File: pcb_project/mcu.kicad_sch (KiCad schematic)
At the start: 24 parts, among them J3 Conn_ST_STDC14, SW2 SW_SPDT, SW3 SW_SPST, U2 STM32U595VJTx, Y1 48MHz

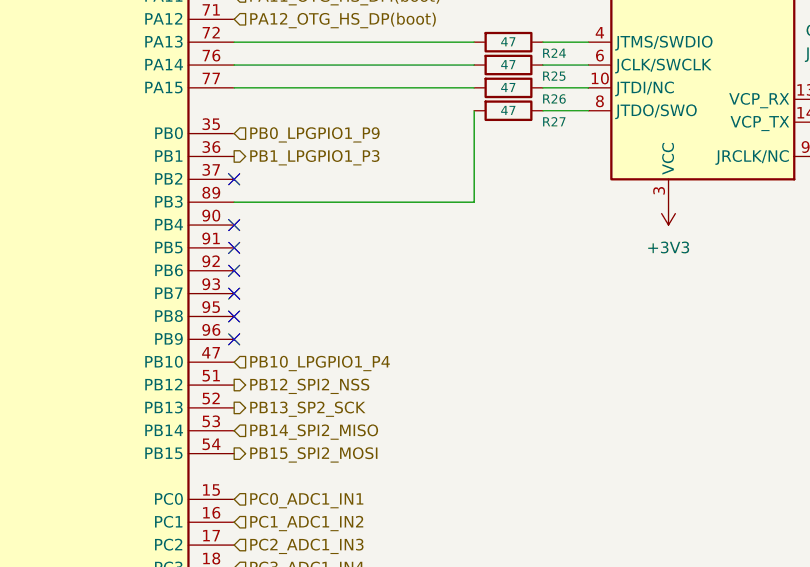
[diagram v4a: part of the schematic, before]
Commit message: Add FPGA DONE AND PROGRAM_B (reset) to MCU GPIO
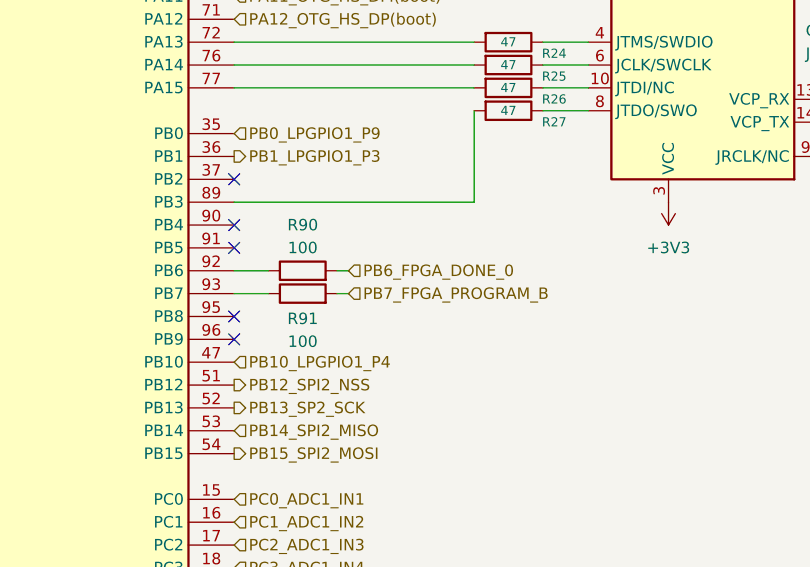
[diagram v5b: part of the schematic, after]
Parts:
- added R90, R91: 100, symbol Device:R
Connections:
- net at U2.92 (PB6): now also R90.1
- net at U2.93 (PB7): now also R91.1
- new net PB6_FPGA_DONE_0: R90.2
- new net PB7_FPGA_PROGRAM_B: R91.2
- no-connect marks 45 -> 43
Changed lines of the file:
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@@
-	)
-	(no_connect
-		(at 124.46 100.33)
 	)
 	(no_connect
@@
 	)
 	(no_connect
-		(at 124.46 97.79)
-	)
-	(no_connect
 		(at 124.46 64.77)
 	)
@@
 	(wire
 		(pts
+			(xy 135.89 97.79) (xy 137.16 97.79)
+		)
+		(stroke
+			(width 0)
+			(type default)
+		)
+	)
+	(wire
+		(pts
 			(xy 73.66 57.15) (xy 78.74 57.15)
 		)
@@
 	(wire
 		(pts
+			(xy 124.46 97.79) (xy 128.27 97.79)
+		)
+		(stroke
+			(width 0)
+			(type default)
+		)
+	)
+	(wire
+		(pts
 			(xy 240.03 36.83) (xy 247.65 36.83)
 		)
@@
 	(wire
 		(pts
+			(xy 124.46 100.33) (xy 128.27 100.33)
+		)
+		(stroke
+			(width 0)
+			(type default)
+		)
+	)
+	(wire
+		(pts
 			(xy 43.18 30.48) (xy 40.64 30.48)
 		)
@@
 		(pts
 			(xy 43.18 39.37) (xy 43.18 30.48)
+		)
+		(stroke
+			(width 0)
+			(type default)
+		)
+	)
+	(wire
+		(pts
+			(xy 135.89 100.33) (xy 137.16 100.33)
 		)
 		(stroke
@@
 		)
 	)
+	(hierarchical_label "PB6_FPGA_DONE_0"
+		(shape input)
+		(at 137.16 97.79 0)
+		(effects
+			(font
+				(size 1.27 1.27)
+			)
+			(justify left)
+		)
+	)
 	(hierarchical_label "PC11_SDMMC1_D3"
 		(shape input)
@@
 			)
 			(justify right)
+		)
+	)
+	(hierarchical_label "PB7_FPGA_PROGRAM_B"
+		(shape input)
+		(at 137.16 100.33 0)
+		(effects
+			(font
+				(size 1.27 1.27)
+			)
+			(justify left)
 		)
 	)
@@
 					(unit 1)
 				)
+			)
+		)
+	)
+	(symbol
+		(lib_id "Device:R")
+		(at 132.08 97.79 90)
+		(unit 1)
+		(exclude_from_sim no)
+		(in_bom yes)
+		(on_board yes)
+		(dnp no)
+		(property "Reference" "R90"
+			(at 132.08 92.71 90)
+			(effects
+				(font
+					(size 1.27 1.27)
+				)
+			)
+		)
+		(property "Value" "100"
+			(at 132.08 95.25 90)
+			(effects
+				(font
+					(size 1.27 1.27)
+				)
+			)
+		)
+		(property "Footprint" ""
+			(at 132.08 99.568 90)
+			(effects
+				(font
+					(size 1.27 1.27)
+				)
+				(hide yes)
+			)
+		)
+		(property "Datasheet" "~"
+			(at 132.08 97.79 0)
+			(effects
+				(font
+					(size 1.27 1.27)
+				)
+				(hide yes)
+			)
+		)
+		(property "Description" "Resistor"
+			(at 132.08 97.79 0)
+			(effects
+				(font
+					(size 1.27 1.27)
+				)
+				(hide yes)
+			)
+		)
+		(pin "1"
+		)
+		(pin "2"
+		)
+		(instances
+			(project ""
+				(path "/98f80f66-4595-4d0f-90ca-59b2db6f447b/1a3eaa4f-d49c-486a-8882-cdef72ae86f4"
+					(reference "R90")
+					(unit 1)
+				)
+			)
+		)
+	)
+	(symbol
+		(lib_id "Device:R")
+		(at 132.08 100.33 90)
+		(unit 1)
+		(exclude_from_sim no)
+		(in_bom yes)
+		(on_board yes)
+		(dnp no)
+		(property "Reference" "R91"
+			(at 132.08 103.124 90)
+			(effects
+				(font
+					(size 1.27 1.27)
+				)
+			)
+		)
+		(property "Value" "100"
+			(at 132.08 105.664 90)
+			(effects
+				(font
+					(size 1.27 1.27)
+				)
+			)
+		)
+		(property "Footprint" ""
+			(at 132.08 102.108 90)
+			(effects
+				(font
+					(size 1.27 1.27)
+				)
+				(hide yes)
+			)
+		)
+		(property "Datasheet" "~"
+			(at 132.08 100.33 0)
+			(effects
+				(font
+					(size 1.27 1.27)
+				)
+				(hide yes)
+			)
+		)
+		(property "Description" "Resistor"
+			(at 132.08 100.33 0)
+			(effects
+				(font
+					(size 1.27 1.27)
+				)
+				(hide yes)
+			)
+		)
+		(pin "1"
+		)
+		(pin "2"
+		)
+		(instances
+			(project ""
+				(path "/98f80f66-4595-4d0f-90ca-59b2db6f447b/1a3eaa4f-d49c-486a-8882-cdef72ae86f4"
+					(reference "R91")
+					(unit 1)
+				)

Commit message: Add most footprints, missing some inductors and 3 buttons
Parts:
- C37, C38: footprint (none) -> Capacitor_SMD:C_0603_1608Metric_Pad1.08x0.95mm_HandSolder
- C39, C41, C42: footprint (none) -> Capacitor_SMD:C_0805_2012Metric_Pad1.18x1.45mm_HandSolder
- C40: footprint (none) -> Capacitor_SMD:C_1206_3216Metric_Pad1.33x1.80mm_HandSolder
- J3: footprint (none) -> Connector_PinHeader_1.27mm:PinHeader_2x07_P1.27mm_Vertical
- R23, R24, R25, R26, R27, R90, R91: footprint (none) -> Resistor_SMD:R_0805_2012Metric_Pad1.20x1.40mm_HandSolder
- Y1: footprint (none) -> Project_Footprints:OSCCC320X250X60N
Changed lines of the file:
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@@
 			)
 		)
-		(property "Footprint" ""
+		(property "Footprint" "Resistor_SMD:R_0805_2012Metric_Pad1.20x1.40mm_HandSolder"
 			(at 154.94 75.692 90)
 			(effects
@@
 			)
 		)
-		(property "Footprint" ""
+		(property "Footprint" "Capacitor_SMD:C_0805_2012Metric_Pad1.18x1.45mm_HandSolder"
 			(at 79.7052 163.83 0)
 			(effects
@@
 			)
 		)
-		(property "Footprint" ""
+		(property "Footprint" "Capacitor_SMD:C_1206_3216Metric_Pad1.33x1.80mm_HandSolder"
 			(at 221.9452 36.83 0)
 			(effects
@@
 			)
 		)
-		(property "Footprint" ""
+		(property "Footprint" "Resistor_SMD:R_0805_2012Metric_Pad1.20x1.40mm_HandSolder"
 			(at 132.08 99.568 90)
 			(effects
@@
 			)
 		)
-		(property "Footprint" ""
+		(property "Footprint" "Resistor_SMD:R_0805_2012Metric_Pad1.20x1.40mm_HandSolder"
 			(at 132.08 102.108 90)
 			(effects
@@
 			)
 		)
-		(property "Footprint" ""
+		(property "Footprint" "Capacitor_SMD:C_0805_2012Metric_Pad1.18x1.45mm_HandSolder"
 			(at 221.9452 83.82 0)
 			(effects
@@
 			)
 		)
-		(property "Footprint" ""
+		(property "Footprint" "Capacitor_SMD:C_0603_1608Metric_Pad1.08x0.95mm_HandSolder"
 			(at 33.02 55.5752 0)
 			(effects
@@
 			)
 		)
-		(property "Footprint" ""
+		(property "Footprint" "Capacitor_SMD:C_0805_2012Metric_Pad1.18x1.45mm_HandSolder"
 			(at 221.9452 60.96 0)
 			(effects
@@
 			)
 		)
-		(property "Footprint" ""
+		(property "Footprint" "Capacitor_SMD:C_0603_1608Metric_Pad1.08x0.95mm_HandSolder"
 			(at 33.02 31.4452 0)
 			(effects
@@
 			)
 		)
-		(property "Footprint" ""
+		(property "Footprint" "Resistor_SMD:R_0805_2012Metric_Pad1.20x1.40mm_HandSolder"
 			(at 154.94 78.232 90)
 			(effects
@@
 			)
 		)
-		(property "Footprint" ""
+		(property "Footprint" "Connector_PinHeader_1.27mm:PinHeader_2x07_P1.27mm_Vertical"
 			(at 176.53 72.39 0)
 			(effects
@@
 			)
 		)
-		(property "Footprint" ""
+		(property "Footprint" "Resistor_SMD:R_0805_2012Metric_Pad1.20x1.40mm_HandSolder"
 			(at 154.94 70.612 90)
 			(effects
@@
 			)
 		)
-		(property "Footprint" ""
+		(property "Footprint" "Resistor_SMD:R_0805_2012Metric_Pad1.20x1.40mm_HandSolder"
 			(at 154.94 73.152 90)
 			(effects
@@
 			)
 		)
-		(property "Footprint" ""
+		(property "Footprint" "Project_Footprints:OSCCC320X250X60N"
 			(at 43.18 43.18 0)
 			(effects
@@
 			)
 		)
-		(property "Footprint" ""
+		(property "Footprint" "Resistor_SMD:R_0805_2012Metric_Pad1.20x1.40mm_HandSolder"
 			(at 69.85 58.928 90)
 			(effects

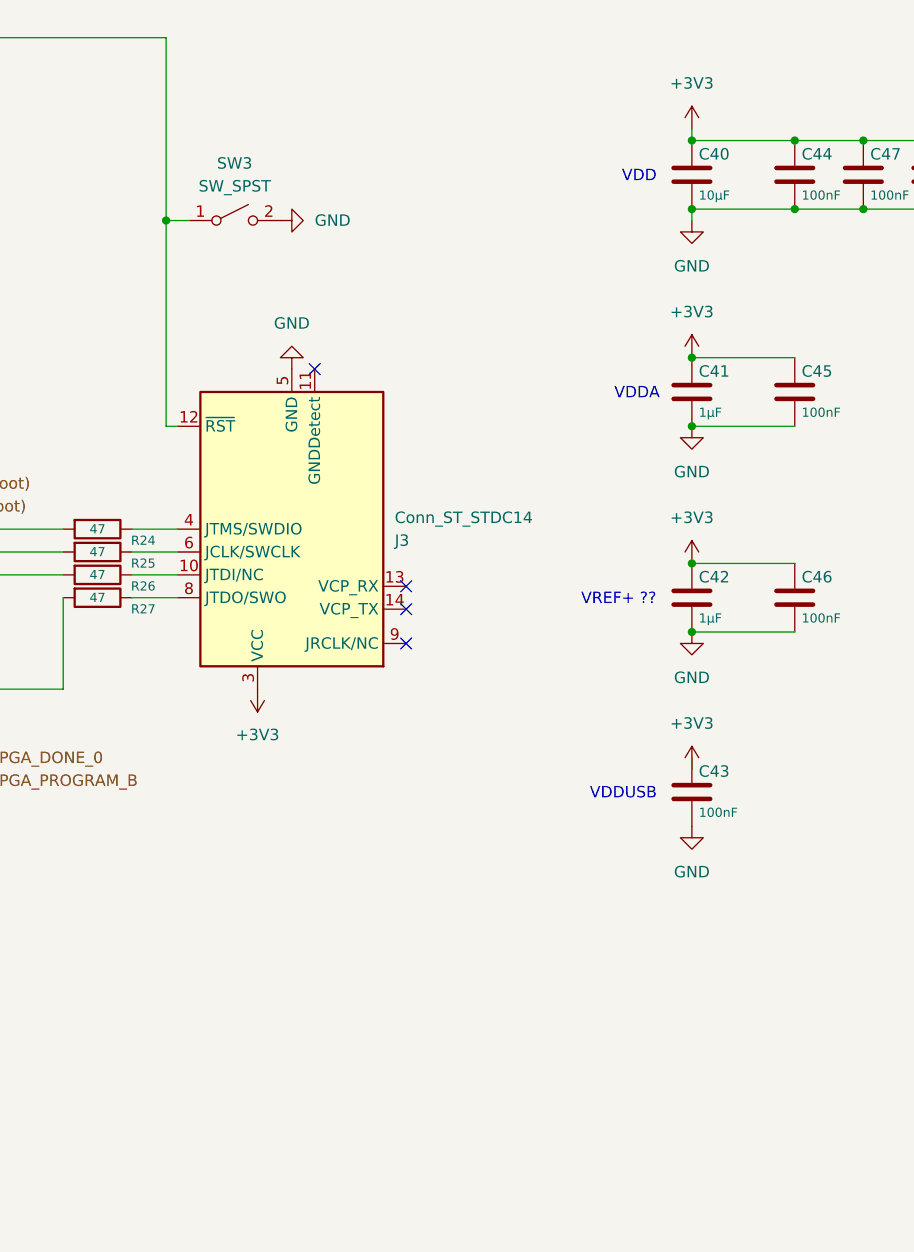
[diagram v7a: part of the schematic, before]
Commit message: Add debouncing capasitor for MCU reset button
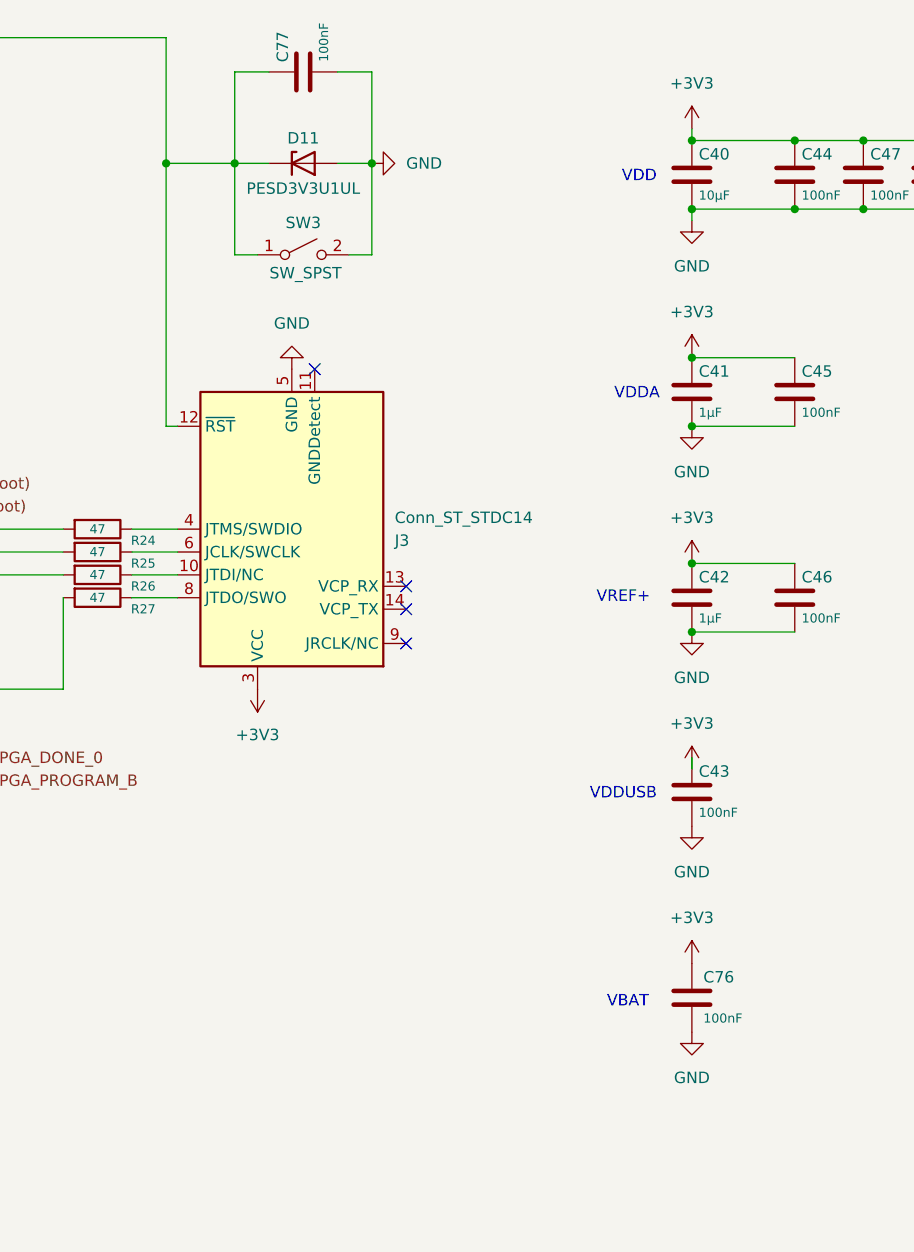
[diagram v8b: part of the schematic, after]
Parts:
- added C76, C77: 100nF, symbol Device:C
- added D11: PESD3V3U1UL, Diode_SMD:D_SOD-882, symbol Diode:PESD3V3U1UL
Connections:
- net +3V3: now also C76.1
- net GND: now also C76.2, C77.2, D11.2 (A)
- net at J3.12 (~{RST}), SW3.1 (A), U2.14 (NRST): now also C77.1, D11.1 (K)
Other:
- note added: "VBAT"
- note added: "VREF+"
- note removed: "VREF+ ??"
- moved on the sheet: SW3
